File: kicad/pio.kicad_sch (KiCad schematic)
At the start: 5 parts, among them J2 DB25_Receptacle_MountingHoles, U2 PIO-DIP-40

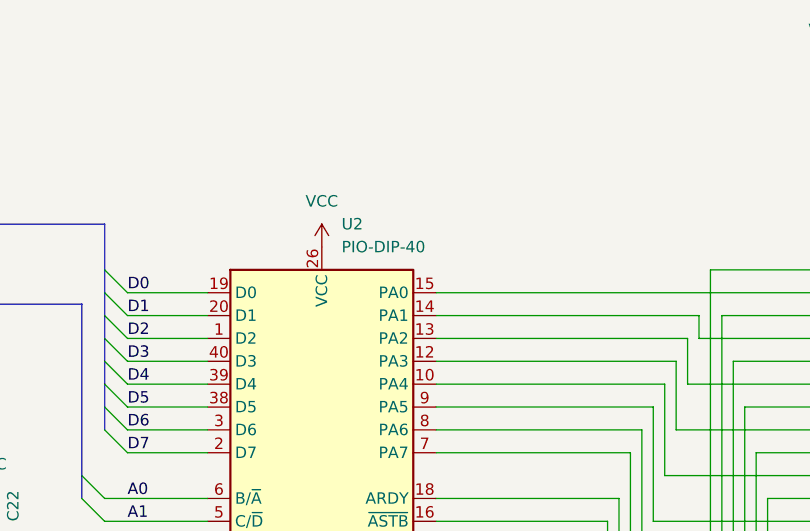
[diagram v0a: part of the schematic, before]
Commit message: HW: Fix A0 of AY-3-8912 being connected to D0 instead of A0
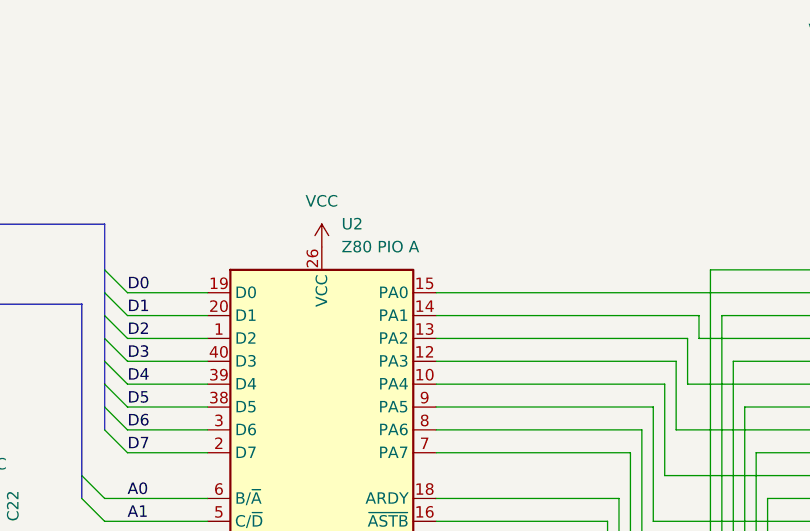
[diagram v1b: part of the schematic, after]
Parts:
- U2: value PIO-DIP-40 -> Z80 PIO A
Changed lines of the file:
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@@
 			)
 		)
-		(property "Value" "PIO-DIP-40"
+		(property "Value" "Z80 PIO A"
 			(at 133.0041 68.58 0)
 			(effects
